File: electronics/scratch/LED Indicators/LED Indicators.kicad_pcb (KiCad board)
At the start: 2 copper layers, 80 x 50 mm, 28 parts, among them J1 POWER INPUT, J2 VLOW TP, J3 VHIGH TP, J4 EXTERNAL LED, J5 EXTERNAL TP, SW1 TS-1187A-B-A-B, SW2 TS-1088-AR02016, SW3 SSSS213202, SW4 TS-1088-AR02016, U5 XL-1608UBC-06A, U6 XL-1608PGC-06

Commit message: Finished LED indicator sch, need to run traces next
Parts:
- added JP10: SolderJumper_2_Bridged, Jumper:SolderJumper-2_P1.3mm_Bridged_RoundedPad1.0x1.5mm, F.Cu at (199.0, 79.0)
- added JP8: SolderJumper_2_Bridged, Jumper:SolderJumper-2_P1.3mm_Bridged_RoundedPad1.0x1.5mm, F.Cu at (199.0, 64.5)
- added JP9: SolderJumper_2_Bridged, Jumper:SolderJumper-2_P1.3mm_Bridged_RoundedPad1.0x1.5mm, F.Cu at (199.0, 71.5)
- added LED1: P2-0603W6YS2-06T-002, easyeda2kicad:LED-SMD_L1.6-W0.8-RD-WHITE-2, F.Cu at (199.0, 66.9)
- added LED2: BL-HJC36G-AV-TRB, easyeda2kicad:LED0603-R-RD_AMBER, F.Cu at (199.0, 74.3)
- added LED3: CT-1608DUPC-P6, easyeda2kicad:LED-SMD_L1.6-W0.8-RD_CT-1608UWC-P4, F.Cu at (199.0, 82.0)
- moved SW4 4.12 mm to (181.5, 95.5), turned to -90 degrees
- moved J5 2.73 mm to (189.9, 96.8), turned to 180 degrees
- moved J4 1.06 mm to (198.4, 96.8)
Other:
- board text added: "BL-HJC36G-AV-TRB"
- board text added: "CT-1608DUPC-P6"
- board text added: "EX ON"
- board text added: "P2-0603W6YS2-06T-002"
- board text added: "TP"
- board text added: "VHIGH ON"
- board text added: "VLOW ON"
- board text removed: "VHIGH LEDS"
- board text removed: "VLOW LEDS"

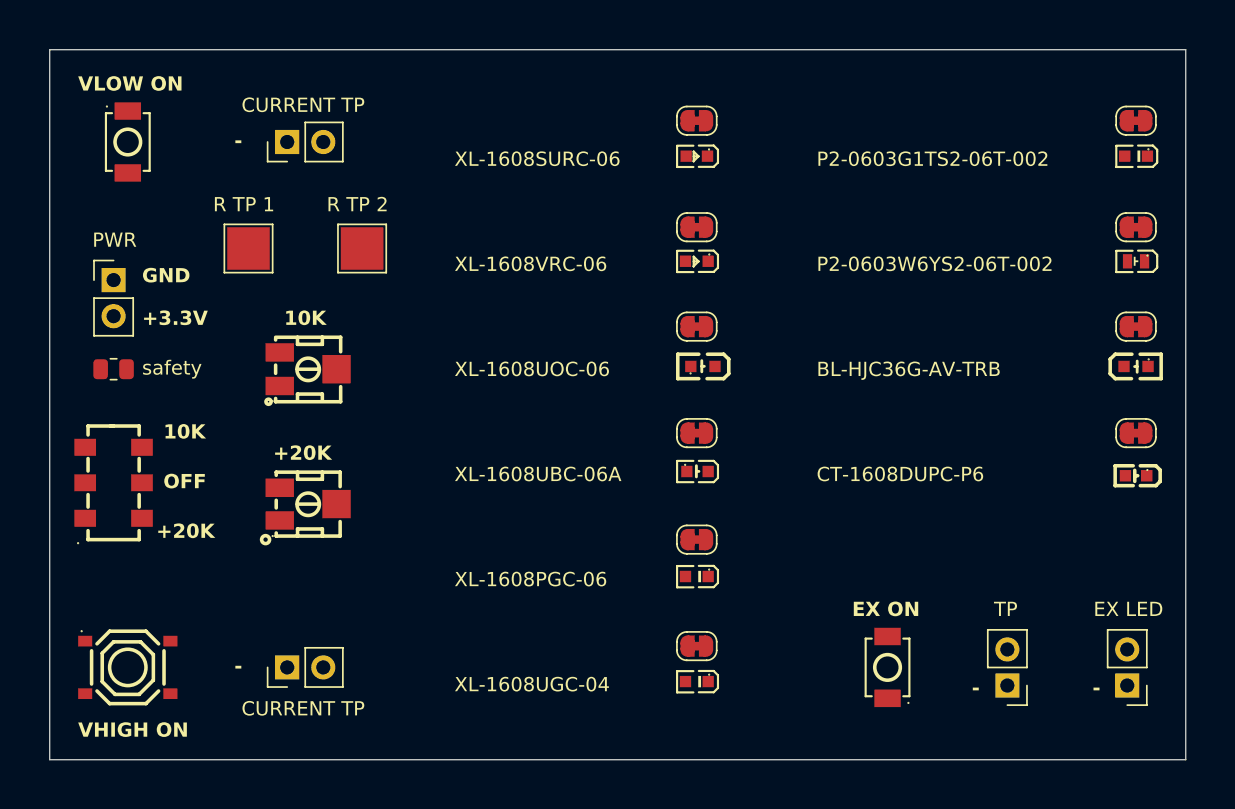
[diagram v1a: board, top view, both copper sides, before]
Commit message: LED indicators board sent to PCBWay for review
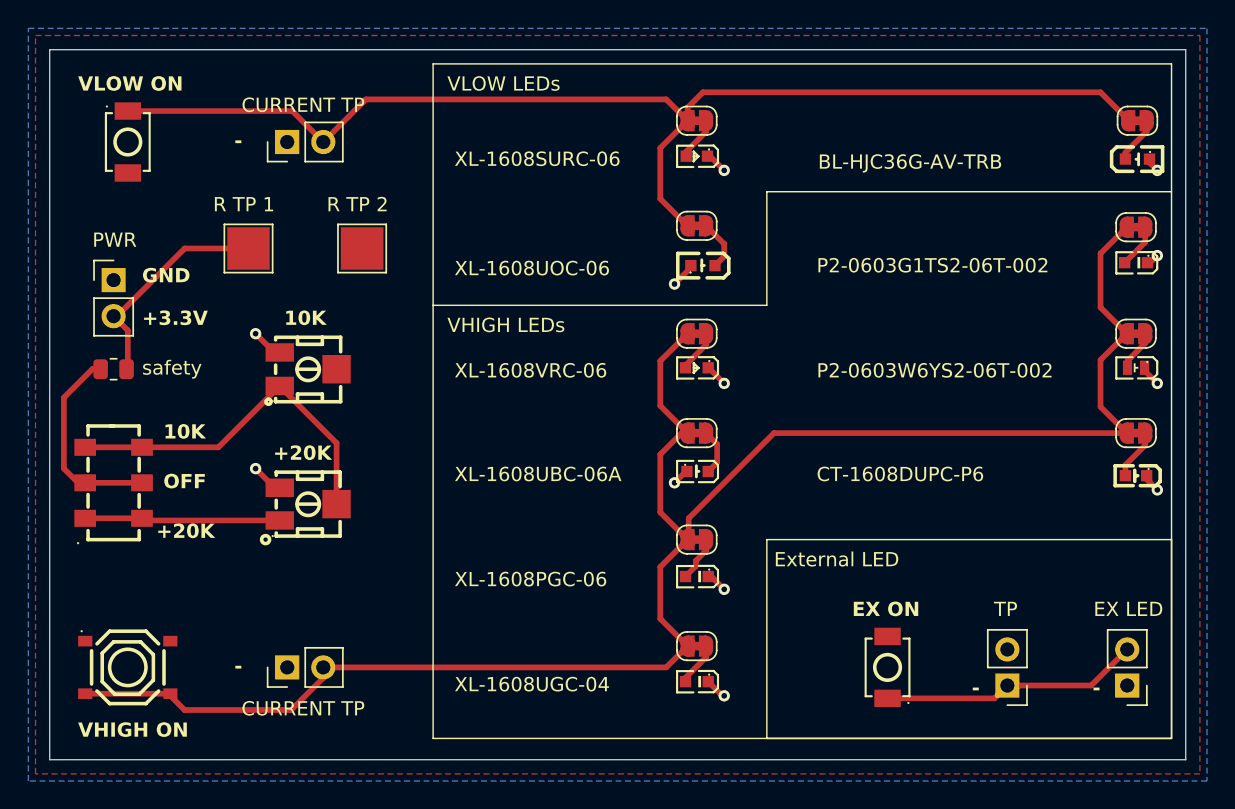
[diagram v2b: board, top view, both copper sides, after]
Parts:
- moved LED2 14.6 mm to (199.1, 59.7)
- moved JP9 14.5 mm to (199.1, 57.0)
- moved JP2 7.50 mm to (168.1, 72.0)
- moved JP7 7.50 mm to (199.0, 64.5)
- moved JP8 7.50 mm to (199.0, 72.0)
- moved LED1 7.50 mm to (199.0, 74.4)
- moved LED10 7.50 mm to (168.1, 74.4)
- moved LED11 7.50 mm to (199.0, 67.0)
- moved LED9 7.10 mm to (168.5, 67.2)
- moved JP3 7.10 mm to (168.1, 64.4)
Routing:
- net +VHIGH: track 0.00 -> 124.7 mm
- net +VLOW: track 0.00 -> 84.4 mm
- net Net-(SW3-Pad3): track 0.00 -> 25.5 mm
- net GND: track 0.00 -> 18.4 mm, vias 0 -> 12
- net Net-(J4-Pin_2): track 0.00 -> 18.3 mm
- net Net-(J1-Pin_2): track 0.00 -> 15.7 mm
- net +VDC: track 0.00 -> 14.3 mm
- net Net-(SW3-Pad1): track 0.00 -> 13.8 mm
- net Net-(JP3-B): track 0.00 -> 3.60 mm
- net Net-(JP10-B): track 0.00 -> 3.58 mm
- net Net-(JP9-B): track 0.00 -> 3.43 mm
- net Net-(JP4-B): track 0.00 -> 3.29 mm
- net Net-(JP2-B): track 0.00 -> 3.22 mm
- net Net-(JP5-B): track 0.00 -> 3.20 mm
- net Net-(JP7-B): track 0.00 -> 3.10 mm
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- added copper zone on F.Cu, net +3.3V
- added copper zone on B.Cu, net GND
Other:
- board text added: "External LED"
- board text added: "VHIGH LEDs"
- board text added: "VLOW LEDs"
